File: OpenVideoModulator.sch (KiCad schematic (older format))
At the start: 22 parts, among them J1 CONN_6, J2 S-Video+Composite_Combo, P1 OSHW_LOGO, U1 AD724, Y1 4.433619M

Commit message: Almost there...
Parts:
- C6: footprint Capacitor_SMD:C_0805_2012Metric_Pad1.15x1.40mm_HandSolder -> Capacitor_SMD:CP_Elec_6.3x5.8
- C7: footprint Capacitor_SMD:C_0805_2012Metric_Pad1.15x1.40mm_HandSolder -> Capacitor_SMD:C_1206_3216Metric_Pad1.42x1.75mm_HandSolder
- JP1: footprint Jumper:SolderJumper-3_P1.3mm_Open_RoundedPad1.0x1.5mm -> OpenVideoModulator:SolderJumper-3_P1.3mm_Bridged12_RoundedPad1.0x1.5mm
- Y1: footprint Crystal:Crystal_HC49-U_Vertical -> Crystal:Crystal_HC49-4H_Vertical
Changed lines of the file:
@@
 Sheet 1 1
 Title "OpenVideoModulator"
-Date "2019-03-16"
+Date "2019-03-21"
 Rev "1git"
 Comp "SukkoPera"
 Comment1 "Inspired from CPC Wiki"
 Comment2 "http://www.cpcwiki.eu/index.php/RGB_SVideo"
-Comment3 ""
+Comment3 "Licensed under CERN OHL v.1.2"
 Comment4 ""
 $EndDescr
@@
 Wire Wire Line
 	6575 3345 6710 3345
-Wire Wire Line
-	4910 4320 4910 4125
 Wire Wire Line
 	4910 3145 5075 3145
@@
 	5075 3345 4820 3345
 Wire Wire Line
-	4820 3345 4820 2475
-Wire Wire Line
-	6710 2475 6710 3145
+	6710 2365 6710 2475
 Wire Wire Line
 	6710 3245 6575 3245
-Wire Wire Line
-	4820 2475 5010 2475
 $Comp
 L power:VCC #PWR07
 U 1 1 5C8D331E
-P 5825 2365
-F 0 "#PWR07" H 5825 2215 50  0001 C CNN
-F 1 "VCC" H 5842 2538 50  0000 C CNN
-F 2 "" H 5825 2365 50  0001 C CNN
-F 3 "" H 5825 2365 50  0001 C CNN
-	1    5825 2365
-	1    0    0    -1
-$EndComp
-Wire Wire Line
-	5825 2365 5825 2475
-Connection ~ 5825 2475
-Wire Wire Line
-	5825 2475 6710 2475
+P 6710 2365
+F 0 "#PWR07" H 6710 2215 50  0001 C CNN
+F 1 "VCC" H 6727 2538 50  0000 C CNN
+F 2 "" H 6710 2365 50  0001 C CNN
+F 3 "" H 6710 2365 50  0001 C CNN
+	1    6710 2365
+	1    0    0    -1
+$EndComp
 $Comp
 L Device:R R4
@@
 F 0 "JP1" V 4540 2955 50  0000 L CNN
 F 1 "NTSC/~PAL" V 4480 3140 50  0000 L CNN
-F 2 "Jumper:SolderJumper-3_P1.3mm_Open_RoundedPad1.0x1.5mm" H 4540 2895 50  0001 C CNN
+F 2 "OpenVideoModulator:SolderJumper-3_P1.3mm_Bridged12_RoundedPad1.0x1.5mm" H 4540 2895 50  0001 C CNN
 F 3 "~" H 4540 2895 50  0001 C CNN
 	1    4540 2895
 	0    -1   -1   0
 $EndComp
-Connection ~ 4820 2475
 Text Notes 4345 3065 0    50   ~ 0
 PAL
@@
 F 0 "Y1" V 3190 3720 50  0000 C CNN
 F 1 "4.433619M" H 3060 3635 50  0000 C CNN
-F 2 "Crystal:Crystal_HC49-U_Vertical" H 3060 3795 50  0001 C CNN
+F 2 "Crystal:Crystal_HC49-4H_Vertical" H 3060 3795 50  0001 C CNN
 F 3 "~" H 3060 3795 50  0001 C CNN
 	1    3060 3795
@@
 	4540 2645 4540 2475
 Wire Wire Line
-	4540 2475 4820 2475
-Wire Wire Line
 	2925 4225 2925 4165
 Connection ~ 2925 4165
@@
 Wire Wire Line
 	5010 3445 5010 2475
-Connection ~ 5010 2475
-Wire Wire Line
-	5010 2475 5825 2475
 Wire Wire Line
 	6575 3145 6710 3145
@@
 	6575 3445 6710 3445
 Connection ~ 6710 3445
-Wire Wire Line
-	6710 3445 6710 4125
 Wire Wire Line
 	6575 3045 7105 3045
@@
 	1    0    0    -1
 $EndComp
-Wire Wire Line
-	4910 4125 5825 4125
-Connection ~ 4910 4125
-Wire Wire Line
-	4910 4125 4910 3145
-Connection ~ 6710 4125
-Wire Wire Line
-	6710 4125 6710 4335
 $Comp
 L power:VAA #PWR09
@@
 	1    0    0    -1
 $EndComp
-$Comp
-L power:GND #PWR08
-U 1 1 5C9698B4
-P 5825 4690
-F 0 "#PWR08" H 5825 4440 50  0001 C CNN
-F 1 "GND" H 5830 4517 50  0000 C CNN
-F 2 "" H 5825 4690 50  0001 C CNN
-F 3 "" H 5825 4690 50  0001 C CNN
-	1    5825 4690
-	1    0    0    -1
-$EndComp
-Wire Wire Line
-	5825 4690 5825 4125
-Connection ~ 5825 4125
-Wire Wire Line
-	5825 4125 6710 4125
 $Comp
 L power:GND #PWR014
@@
 	-1   0    0    1
 $EndComp
-$Comp
-L power:PWR_FLAG #FLG01
-U 1 1 5C96BD29
-P 10060 935
-F 0 "#FLG01" H 10060 1010 50  0001 C CNN
-F 1 "PWR_FLAG" H 10060 1108 50  0000 C CNN
-F 2 "" H 10060 935 50  0001 C CNN
-F 3 "~" H 10060 935 50  0001 C CNN
-	1    10060 935
-	-1   0    0    1
-$EndComp
 Wire Wire Line
 	10825 840  10825 935
 Wire Wire Line
 	10435 835  10435 935
-Wire Wire Line
-	10060 840  10060 935
 $Comp
 L power:GNDA #PWR010
@@
 F 0 "C6" H 6020 7115 50  0000 C CNN
 F 1 "100u" V 6000 6840 50  0000 C CNN
-F 2 "Capacitor_SMD:C_0805_2012Metric_Pad1.15x1.40mm_HandSolder" H 5950 7015 50  0001 C CNN
+F 2 "Capacitor_SMD:CP_Elec_6.3x5.8" H 5950 7015 50  0001 C CNN
 F 3 "~" H 5950 7015 50  0001 C CNN
 	1    5950 7015
@@
 F 0 "C7" H 6175 6915 50  0000 C CNN
 F 1 "100n" V 6190 7180 50  0000 C CNN
-F 2 "Capacitor_SMD:C_0805_2012Metric_Pad1.15x1.40mm_HandSolder" H 6288 6865 50  0001 C CNN
+F 2 "Capacitor_SMD:C_1206_3216Metric_Pad1.42x1.75mm_HandSolder" H 6288 6865 50  0001 C CNN
 F 3 "~" H 6250 7015 50  0001 C CNN
 	1    6250 7015
@@
 L power:VCC #PWR0101
 U 1 1 5C99C960
-P 10060 840
-F 0 "#PWR0101" H 10060 690 50  0001 C CNN
-F 1 "VCC" H 10077 1013 50  0000 C CNN
-F 2 "" H 10060 840 50  0001 C CNN
-F 3 "" H 10060 840 50  0001 C CNN
-	1    10060 840
+P 1020 6735
+F 0 "#PWR0101" H 1020 6585 50  0001 C CNN
+F 1 "VCC" H 1037 6908 50  0000 C CNN
+F 2 "" H 1020 6735 50  0001 C CNN
+F 3 "" H 1020 6735 50  0001 C CNN
+	1    1020 6735
 	1    0    0    -1
 $EndComp
@@
 L power:VAA #PWR0102
 U 1 1 5C99CBD3
-P 10435 835
-F 0 "#PWR0102" H 10435 685 50  0001 C CNN
-F 1 "VAA" H 10452 1008 50  0000 C CNN
-F 2 "" H 10435 835 50  0001 C CNN
-F 3 "" H 10435 835 50  0001 C CNN
-	1    10435 835
+P 1395 6730
+F 0 "#PWR0102" H 1395 6580 50  0001 C CNN
+F 1 "VAA" H 1412 6903 50  0000 C CNN
+F 2 "" H 1395 6730 50  0001 C CNN
+F 3 "" H 1395 6730 50  0001 C CNN
+	1    1395 6730
 	1    0    0    -1
 $EndComp
@@
 	1    0    0    -1
 $EndComp
+$Comp
+L power:VAA #PWR0103
+U 1 1 5C973F8B
+P 4820 2365
+F 0 "#PWR0103" H 4820 2215 50  0001 C CNN
+F 1 "VAA" H 4837 2538 50  0000 C CNN
+F 2 "" H 4820 2365 50  0001 C CNN
+F 3 "" H 4820 2365 50  0001 C CNN
+	1    4820 2365
+	1    0    0    -1
+$EndComp
+Wire Wire Line
+	5010 2475 6710 2475
+Connection ~ 6710 2475
+Wire Wire Line
+	6710 2475 6710 3145
+Wire Wire Line
+	4820 2365 4820 3345
+Wire Wire Line
+	4540 2475 5010 2475
+Connection ~ 5010 2475
+Wire Wire Line
+	1020 6735 1020 6830
+Wire Wire Line
+	1020 6830 1395 6830
+Wire Wire Line
+	1395 6830 1395 6730
+Wire Wire Line
+	880  7200 880  7005
+$Comp
+L power:GNDA #PWR0104
+U 1 1 5C992824
+P 880 7200
+F 0 "#PWR0104" H 880 6950 50  0001 C CNN
+F 1 "GNDA" H 885 7027 50  0000 C CNN
+F 2 "" H 880 7200 50  0001 C CNN
+F 3 "" H 880 7200 50  0001 C CNN
+	1    880  7200
+	1    0    0    -1
+$EndComp
+$Comp
+L power:GNDD #PWR0105
+U 1 1 5C99282A
+P 1515 7215
+F 0 "#PWR0105" H 1515 6965 50  0001 C CNN
+F 1 "GNDD" H 1519 7060 50  0000 C CNN
+F 2 "" H 1515 7215 50  0001 C CNN
+F 3 "" H 1515 7215 50  0001 C CNN
+	1    1515 7215
+	1    0    0    -1
+$EndComp
+Wire Wire Line
+	880  7005 1205 7005
+Wire Wire Line
+	1515 7005 1515 7215
+$Comp
+L power:GND #PWR0106
+U 1 1 5C992835
+P 1205 7395
+F 0 "#PWR0106" H 1205 7145 50  0001 C CNN
+F 1 "GND" H 1210 7222 50  0000 C CNN
+F 2 "" H 1205 7395 50  0001 C CNN
+F 3 "" H 1205 7395 50  0001 C CNN
+	1    1205 7395
+	1    0    0    -1
+$EndComp
+Wire Wire Line
+	1205 7395 1205 7005
+Connection ~ 1205 7005
+Wire Wire Line
+	1205 7005 1515 7005
+Wire Wire Line
+	4910 3145 4910 4320
+Wire Wire Line
+	6710 3445 6710 4335
+$Comp
+L power:VCC #PWR0107
+U 1 1 5C9C2114
+P 10435 835
+F 0 "#PWR0107" H 10435 685 50  0001 C CNN
+F 1 "VCC" H 10452 1008 50  0000 C CNN
+F 2 "" H 10435 835 50  0001 C CNN
+F 3 "" H 10435 835 50  0001 C CNN
+	1    10435 835
+	1    0    0    -1
+$EndComp

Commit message: Use 6.3mm electrolytics, as 220uF seem to be more common this size At least >= 16V models, which are recommended
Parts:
- C10, C8, C9: footprint Capacitor_THT:CP_Radial_D5.0mm_P2.00mm -> Capacitor_THT:CP_Radial_D6.3mm_P2.50mm
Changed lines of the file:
@@
 F 0 "C10" V 7460 4295 50  0000 C CNN
 F 1 "220u" V 7460 3990 50  0000 C CNN
-F 2 "Capacitor_THT:CP_Radial_D5.0mm_P2.00mm" H 7410 4165 50  0001 C CNN
+F 2 "Capacitor_THT:CP_Radial_D6.3mm_P2.50mm" H 7410 4165 50  0001 C CNN
 F 3 "~" H 7410 4165 50  0001 C CNN
 	1    7410 4165
@@
 F 0 "C9" V 7460 4085 50  0000 C CNN
 F 1 "220u" V 7460 3780 50  0000 C CNN
-F 2 "Capacitor_THT:CP_Radial_D5.0mm_P2.00mm" H 7410 3955 50  0001 C CNN
+F 2 "Capacitor_THT:CP_Radial_D6.3mm_P2.50mm" H 7410 3955 50  0001 C CNN
 F 3 "~" H 7410 3955 50  0001 C CNN
 	1    7410 3955
@@
 F 0 "C8" V 7460 3565 50  0000 C CNN
 F 1 "220u" V 7460 3260 50  0000 C CNN
-F 2 "Capacitor_THT:CP_Radial_D5.0mm_P2.00mm" H 7410 3435 50  0001 C CNN
+F 2 "Capacitor_THT:CP_Radial_D6.3mm_P2.50mm" H 7410 3435 50  0001 C CNN
 F 3 "~" H 7410 3435 50  0001 C CNN
 	1    7410 3435

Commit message: Ground S-Video connector shielding... AND READY FOR V1!
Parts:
- added unit 3 of J2
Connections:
- wire segments 113 -> 115
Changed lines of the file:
@@
 	7025 3435 7260 3435
 Wire Wire Line
-	8760 3710 8760 3635
+	8760 3710 8760 3670
 $Comp
 L s-video+composite_combo:S-Video+Composite_Combo J2
@@
 	1    0    0    -1
 $EndComp
+$Comp
+L s-video+composite_combo:S-Video+Composite_Combo J2
+U 3 1 5CA00AEA
+P 8905 3670
+F 0 "J2" H 8955 3780 50  0000 C CNN
+F 1 "S-Video+Composite_Combo" H 9044 3804 50  0001 C CNN
+F 2 "" H 8905 3520 50  0001 C CNN
+F 3 "" H 8905 3520 50  0001 C CNN
+	3    8905 3670
+	1    0    0    -1
+$EndComp
+Wire Wire Line
+	8905 3670 8760 3670
+Connection ~ 8760 3670
+Wire Wire Line
+	8760 3670 8760 3635
 $EndSCHEMATC

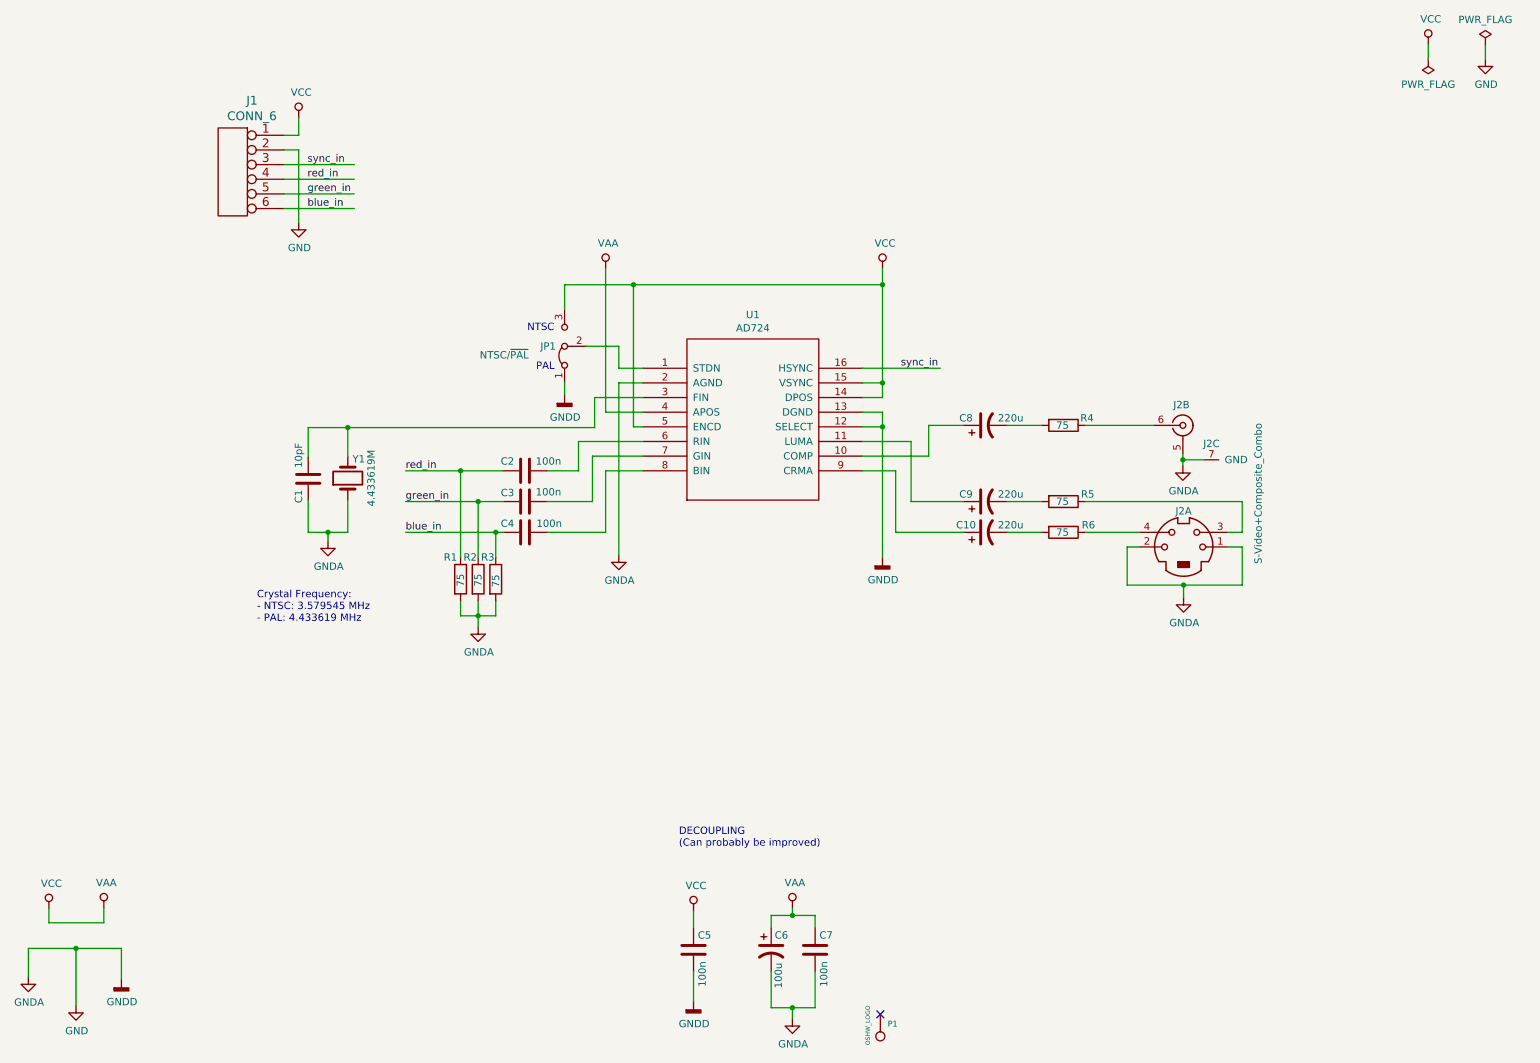
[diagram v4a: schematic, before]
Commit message: V2 with RCA connector for composite video only
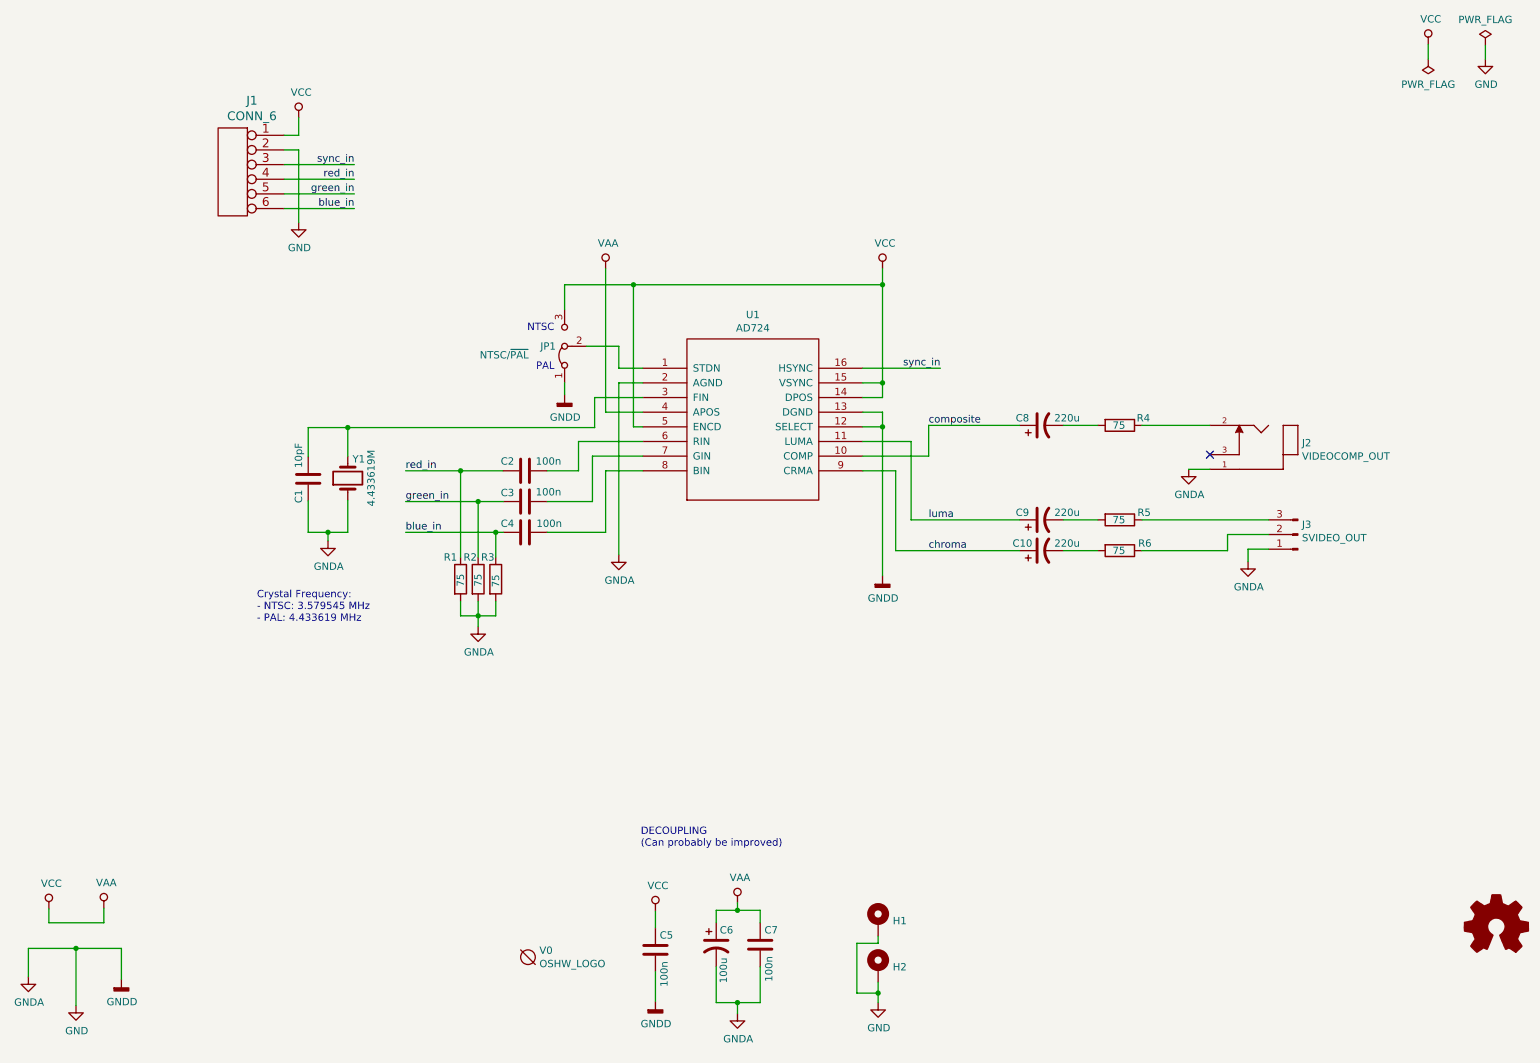
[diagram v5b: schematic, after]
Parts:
- removed J2: S-Video+Composite_Combo, OpenVideoModulator:AV-MDC-401, symbol s-video+composite_combo:S-Video+Composite_Combo
- removed P1: OSHW_LOGO, Symbol:OSHW-Logo2_7.3x6mm_Copper, symbol conn:CONN_1
- added H1, H2: MountingHole_Pad, MountingHole:MountingHole_3.2mm_M3_Pad, symbol Mechanical:MountingHole_Pad
- added J2: VIDEOCOMP_OUT, OpenVideoModulator:SWITCHCRAFT_PJRAN1X1U01X, symbol PJRAN1X1U01X:PJRAN1X1U01X
- added J3: SVIDEO_OUT, OpenVideoModulator:Pin_Header_Straight_1x03-ModSilkS, symbol Connector:Conn_01x03_Male
- added V0: OSHW_LOGO, OpenVideoModulator:oshw_logo, symbol void:Void
- J1: footprint Connector_PinHeader_2.54mm:PinHeader_1x06_P2.54mm_Vertical -> OpenVideoModulator:PinHeader_1x06_P2.54mm_Vertical
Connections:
- net labels added: chroma, composite, luma
- wire segments 115 -> 114
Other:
- moved on the sheet: C10, C5, C6, C7, C8, C9, R4, R5, R6

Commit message: Rename J2
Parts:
- J2: value VIDEOCOMP_OUT -> COMPVIDEO_OUT
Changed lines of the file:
@@
 P 9245 3635
 F 0 "J2" H 8917 3715 50  0000 R CNN
-F 1 "VIDEOCOMP_OUT" H 8917 3624 50  0000 R CNN
+F 1 "COMPVIDEO_OUT" H 8917 3624 50  0000 R CNN
 F 2 "OpenVideoModulator:SWITCHCRAFT_PJRAN1X1U01X" H 9245 3635 50  0001 L BNN
 F 3 "A" H 9245 3635 50  0001 L BNN
